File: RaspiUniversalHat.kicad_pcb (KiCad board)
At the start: 2 copper layers, 56.6 x 65.5 mm, 59 parts, among them J1 Raspberry_Pi_2_3, J10 Conn_01x05, J12 Conn_01x05, J13 Conn_01x05, J15 Conn_01x05, J16 Conn_01x05, J17 Conn_01x05, J18 Conn_01x05, J19 Conn_01x05, J2 Conn_01x20, J21 Conn_01x05, J22 Conn_01x05, J23 Conn_01x05, J24 Conn_01x05, J25 Conn_01x05, J26 Conn_01x05, J27 Conn_01x05, J28 Conn_01x05, J29 Conn_01x05, J3 Conn_01x20, J30 Conn_01x05, J32 Conn_01x05, J33 Conn_01x05, J34 Conn_01x05, J35 Conn_01x05, J36 Conn_01x05, J37 Conn_01x05, J38 Conn_01x05, J39 Conn_01x05, J4 Conn_01x05, J40 Conn_01x05, J41 Conn_01x05, J42 Conn_01x05, J43 Conn_01x05, J44 Conn_01x05, J45 Conn_01x05, J46 Conn_01x05, J47 Conn_01x05, J48 Conn_01x05, J49 Conn_01x05, J5 Conn_01x05, J50 Conn_01x05, J51 Conn_01x05, J52 Conn_01x05, J53 Conn_01x05, J54 Conn_01x05, J55 Conn_01x05, J57 Conn_01x05, J58 Conn_01x05, J59 Conn_01x05, J61 Conn_01x05, J62 Conn_01x05, J63 Conn_01x05, J64 Conn_01x05, J9 Conn_01x05

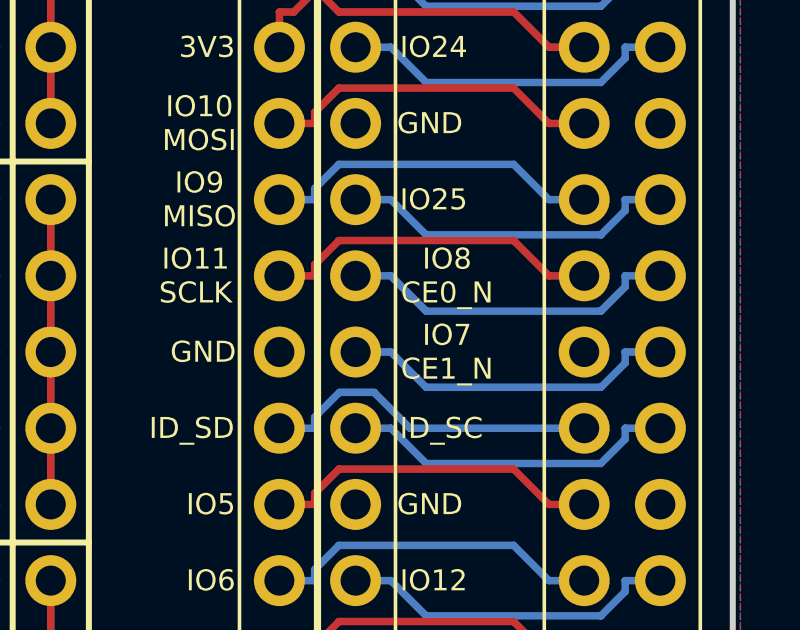
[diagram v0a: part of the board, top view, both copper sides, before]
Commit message: Update text on silk
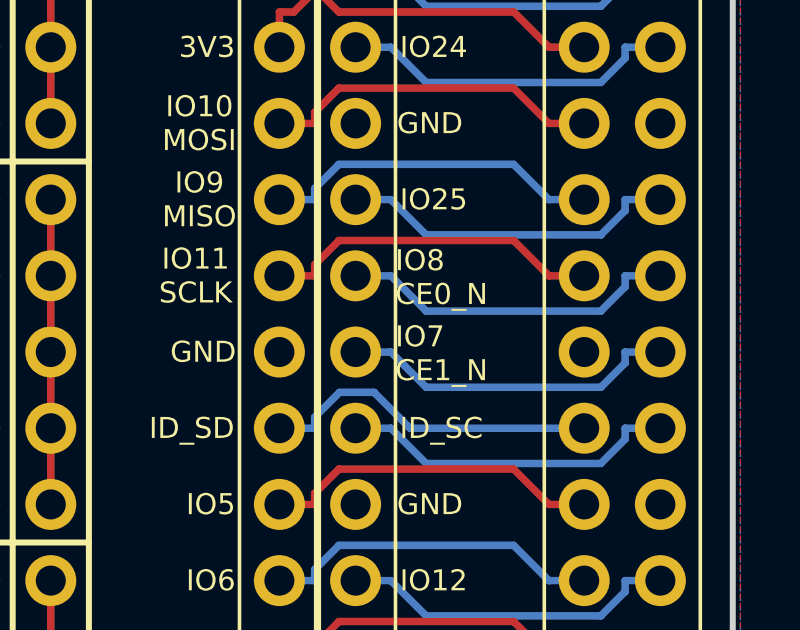
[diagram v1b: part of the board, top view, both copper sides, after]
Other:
- board text added: "github.com/asukiaaa/RaspiUniversalHat"
- board text removed: "github.com/asukiaaa/RaspiUnibersalHat"
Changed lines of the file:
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@@
     (effects (font (size 0.7 0.7) (thickness 0.175)))
   )
-  (gr_text "IO8\nCE0_N" (at 119.38 104.14) (layer F.SilkS)
-    (effects (font (size 0.7 0.7) (thickness 0.175)))
+  (gr_text "IO8\nCE0_N" (at 117.6528 104.1908) (layer F.SilkS)
+    (effects (font (size 0.7 0.7) (thickness 0.175)) (justify left))
   )
   (gr_text GND (at 118.8085 91.44) (layer F.SilkS)
@@
     (effects (font (size 0.7 0.7) (thickness 0.175)))
   )
-  (gr_text "IO7\nCE1_N" (at 119.38 106.68) (layer F.SilkS)
-    (effects (font (size 0.7 0.7) (thickness 0.175)))
+  (gr_text "IO7\nCE1_N" (at 117.6528 106.7308) (layer F.SilkS)
+    (effects (font (size 0.7 0.7) (thickness 0.175)) (justify left))
   )
-  (gr_text "github.com/asukiaaa/RaspiUnibersalHat\n" (at 100.457 131.191) (layer B.SilkS)
+  (gr_text "github.com/asukiaaa/RaspiUniversalHat\n" (at 100.457 131.191) (layer B.SilkS)
     (effects (font (size 1 1) (thickness 0.25)) (justify mirror))
   )

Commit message: Apply large clearance mounting holes
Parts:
- REF1, REF2, REF3, REF4: footprint MountingHole:MountingHole_2.7mm -> Footprints:LargeClearanceMountingHole_2.7mm
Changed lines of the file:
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@@
     (mod_text_size 1 1)
     (mod_text_width 0.15)
-    (pad_size 5.4 5.4)
+    (pad_size 2.7 2.7)
     (pad_drill 2.7)
     (pad_to_mask_clearance 0.2)
@@
     (add_net "Net-(J9-Pad1)")
   )
+  (module Footprints:LargeClearanceMountingHole_2.7mm (layer F.Cu)
+    (at 76.095 129.33)
+    (descr "Mounting Hole 2.7mm, no annular")
+    (tags "mounting hole 2.7mm no annular")
+    (attr virtual)
+    (fp_text reference REF4 (at 0 -3.7) (layer F.SilkS) hide
+      (effects (font (size 1 1) (thickness 0.15)))
+    )
+    (fp_text value MountingHole_2.7mm (at 0 3.7) (layer F.Fab) hide
+      (effects (font (size 1 1) (thickness 0.15)))
+    )
+    (fp_circle (center 0 0) (end 2.95 0) (layer F.CrtYd) (width 0.05))
+    (fp_circle (center 0 0) (end 2.7 0) (layer Cmts.User) (width 0.15))
+    (fp_text user %R (at 0.3 0) (layer F.Fab)
+      (effects (font (size 1 1) (thickness 0.15)))
+    )
+    (pad "" np_thru_hole circle (at 0 0) (size 2.7 2.7) (drill 2.7) (layers *.Cu *.Mask)
+      (solder_mask_margin 1.3) (clearance 1.6))
+  )
+  (module Footprints:LargeClearanceMountingHole_2.7mm (layer F.Cu)
+    (at 125.095 129.33)
+    (descr "Mounting Hole 2.7mm, no annular")
+    (tags "mounting hole 2.7mm no annular")
+    (attr virtual)
+    (fp_text reference REF3 (at 0 -3.7) (layer F.SilkS) hide
+      (effects (font (size 1 1) (thickness 0.15)))
+    )
+    (fp_text value MountingHole_2.7mm (at 0 3.7) (layer F.Fab) hide
+      (effects (font (size 1 1) (thickness 0.15)))
+    )
+    (fp_circle (center 0 0) (end 2.95 0) (layer F.CrtYd) (width 0.05))
+    (fp_circle (center 0 0) (end 2.7 0) (layer Cmts.User) (width 0.15))
+    (fp_text user %R (at 0.3 0) (layer F.Fab)
+      (effects (font (size 1 1) (thickness 0.15)))
+    )
+    (pad "" np_thru_hole circle (at 0 0) (size 2.7 2.7) (drill 2.7) (layers *.Cu *.Mask)
+      (solder_mask_margin 1.3) (clearance 1.6))
+  )
+  (module Footprints:LargeClearanceMountingHole_2.7mm (layer F.Cu)
+    (at 76.095 71.33)
+    (descr "Mounting Hole 2.7mm, no annular")
+    (tags "mounting hole 2.7mm no annular")
+    (attr virtual)
+    (fp_text reference REF1 (at 0 -3.7) (layer F.SilkS) hide
+      (effects (font (size 1 1) (thickness 0.15)))
+    )
+    (fp_text value MountingHole_2.7mm (at 0 3.7) (layer F.Fab) hide
+      (effects (font (size 1 1) (thickness 0.15)))
+    )
+    (fp_circle (center 0 0) (end 2.95 0) (layer F.CrtYd) (width 0.05))
+    (fp_circle (center 0 0) (end 2.7 0) (layer Cmts.User) (width 0.15))
+    (fp_text user %R (at 0.3 0) (layer F.Fab)
+      (effects (font (size 1 1) (thickness 0.15)))
+    )
+    (pad "" np_thru_hole circle (at 0 0) (size 2.7 2.7) (drill 2.7) (layers *.Cu *.Mask)
+      (solder_mask_margin 1.3) (clearance 1.6))
+  )
+  (module Footprints:LargeClearanceMountingHole_2.7mm (layer F.Cu)
+    (at 125.095 71.33)
+    (descr "Mounting Hole 2.7mm, no annular")
+    (tags "mounting hole 2.7mm no annular")
+    (attr virtual)
+    (fp_text reference REF2 (at 0 -3.7) (layer F.SilkS) hide
+      (effects (font (size 1 1) (thickness 0.15)))
+    )
+    (fp_text value MountingHole_2.7mm (at 0 3.7) (layer F.Fab) hide
+      (effects (font (size 1 1) (thickness 0.15)))
+    )
+    (fp_circle (center 0 0) (end 2.95 0) (layer F.CrtYd) (width 0.05))
+    (fp_circle (center 0 0) (end 2.7 0) (layer Cmts.User) (width 0.15))
+    (fp_text user %R (at 0.3 0) (layer F.Fab)
+      (effects (font (size 1 1) (thickness 0.15)))
+    )
+    (pad "" np_thru_hole circle (at 0 0) (size 2.7 2.7) (drill 2.7) (layers *.Cu *.Mask)
+      (solder_mask_margin 1.3) (clearance 1.6))
+  )
   (module Footprints:NoMarkedPinSocket_1x05_P2.54mm (layer F.Cu)
     (at 80.772 114.3)
@@
     )
   )
-  (module MountingHole:MountingHole_2.7mm (layer F.Cu)
-    (at 76.095 71.33)
-    (descr "Mounting Hole 2.7mm, no annular")
-    (tags "mounting hole 2.7mm no annular")
-    (attr virtual)
-    (fp_text reference REF1 (at 0 -3.7) (layer F.SilkS) hide
-      (effects (font (size 1 1) (thickness 0.15)))
-    )
-    (fp_text value MountingHole_2.7mm (at 0 3.7) (layer F.Fab) hide
-      (effects (font (size 1 1) (thickness 0.15)))
-    )
-    (fp_circle (center 0 0) (end 2.95 0) (layer F.CrtYd) (width 0.05))
-    (fp_circle (center 0 0) (end 2.7 0) (layer Cmts.User) (width 0.15))
-    (fp_text user %R (at 0.343 -0.007) (layer F.Fab)
-      (effects (font (size 1 1) (thickness 0.15)))
-    )
-    (pad 1 np_thru_hole circle (at 0 0) (size 2.7 2.7) (drill 2.7) (layers *.Cu *.Mask))
-  )
-  (module MountingHole:MountingHole_2.7mm (layer F.Cu)
-    (at 125.095 71.33)
-    (descr "Mounting Hole 2.7mm, no annular")
-    (tags "mounting hole 2.7mm no annular")
-    (attr virtual)
-    (fp_text reference REF2 (at 0 -3.7) (layer F.SilkS) hide
-      (effects (font (size 1 1) (thickness 0.15)))
-    )
-    (fp_text value MountingHole_2.7mm (at 0 3.7) (layer F.Fab) hide
-      (effects (font (size 1 1) (thickness 0.15)))
-    )
-    (fp_circle (center 0 0) (end 2.95 0) (layer F.CrtYd) (width 0.05))
-    (fp_circle (center 0 0) (end 2.7 0) (layer Cmts.User) (width 0.15))
-    (fp_text user %R (at 0.3 0) (layer F.Fab)
-      (effects (font (size 1 1) (thickness 0.15)))
-    )
-    (pad 1 np_thru_hole circle (at 0 0) (size 2.7 2.7) (drill 2.7) (layers *.Cu *.Mask))
-  )
-  (module MountingHole:MountingHole_2.7mm (layer F.Cu)
-    (at 76.095 129.33)
-    (descr "Mounting Hole 2.7mm, no annular")
-    (tags "mounting hole 2.7mm no annular")
-    (attr virtual)
-    (fp_text reference REF4 (at 0 -3.7) (layer F.SilkS) hide
-      (effects (font (size 1 1) (thickness 0.15)))
-    )
-    (fp_text value MountingHole_2.7mm (at 0 3.7) (layer F.Fab) hide
-      (effects (font (size 1 1) (thickness 0.15)))
-    )
-    (fp_circle (center 0 0) (end 2.95 0) (layer F.CrtYd) (width 0.05))
-    (fp_circle (center 0 0) (end 2.7 0) (layer Cmts.User) (width 0.15))
-    (fp_text user %R (at 0.3 0) (layer F.Fab)
-      (effects (font (size 1 1) (thickness 0.15)))
-    )
-    (pad 1 np_thru_hole circle (at 0 0) (size 2.7 2.7) (drill 2.7) (layers *.Cu *.Mask))
-  )
-  (module MountingHole:MountingHole_2.7mm (layer F.Cu)
-    (at 125.095 129.33)
-    (descr "Mounting Hole 2.7mm, no annular")
-    (tags "mounting hole 2.7mm no annular")
-    (attr virtual)
-    (fp_text reference REF3 (at 0 -3.7) (layer F.SilkS) hide
-      (effects (font (size 1 1) (thickness 0.15)))
-    )
-    (fp_text value MountingHole_2.7mm (at 0 3.7) (layer F.Fab) hide
-      (effects (font (size 1 1) (thickness 0.15)))
-    )
-    (fp_circle (center 0 0) (end 2.95 0) (layer F.CrtYd) (width 0.05))
-    (fp_circle (center 0 0) (end 2.7 0) (layer Cmts.User) (width 0.15))
-    (fp_text user %R (at 0.3 0) (layer F.Fab)
-      (effects (font (size 1 1) (thickness 0.15)))
-    )
-    (pad 1 np_thru_hole circle (at 0 0) (size 2.7 2.7) (drill 2.7) (layers *.Cu *.Mask))
-  )
   (module Footprints:NoMarkedPinSocket_1x05_P2.54mm (layer F.Cu)
